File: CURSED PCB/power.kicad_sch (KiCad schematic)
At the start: 21 parts, among them J3 2 Wire Block for laser, J5 G125-MH104M4-04AD000P, U2 INA180, U4 SPX3819M5-L-3-3, U5 MCP1754S-3302xCB

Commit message: Small changes
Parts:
- F1: value 2A -> 1A
- J5: footprint canhw_footprints:HARWIN_G125-MH104M4-04AD000P -> canhw_footprints:connector_Harwin_G125-MH104M4-04AD000P
- gave numbers to parts that had none: 1
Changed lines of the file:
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@@
 			)
 		)
-		(property "Value" "2A"
+		(property "Value" "1A"
 			(at 53.34 53.34 90)
 			(effects
@@
 		(dnp no)
 		(fields_autoplaced yes)
-		(property "Reference" "U?"
+		(property "Reference" "U1"
 			(at 46.99 99.06 0)
 			(effects
@@
 			(project ""
 				(path "/9fb1a86f-679c-4b88-9ed1-932f4f414580/78e664bb-f661-4ad0-951c-8ffe0c2483d0"
-					(reference "U?")
+					(reference "U1")
 					(unit 1)
 				)
@@
 			)
 		)
-		(property "Footprint" "canhw_footprints:HARWIN_G125-MH104M4-04AD000P"
+		(property "Footprint" "canhw_footprints:connector_Harwin_G125-MH104M4-04AD000P"
 			(at 26.67 48.26 0)
 			(effects

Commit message: file
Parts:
- C10, C11, C12, C13, C8, C9: footprint Capacitor_SMD:C_0201_0603Metric_Pad0.64x0.40mm_HandSolder -> Capacitor_SMD:C_0603_1608Metric_Pad1.08x0.95mm_HandSolder
- R6: footprint Resistor_SMD:R_0201_0603Metric -> Resistor_SMD:R_0603_1608Metric_Pad0.98x0.95mm_HandSolder
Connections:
- net +3.3V is gone; now on net +3.3VD: U2.5 (V+)
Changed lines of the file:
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@@
 	)
 	(junction
-		(at 118.11 57.15)
-		(diameter 0)
-		(color 0 0 0 0)
-	)
-	(junction
 		(at 205.74 88.9)
 		(diameter 0)
@@
 	(wire
 		(pts
-			(xy 118.11 46.99) (xy 118.11 57.15)
+			(xy 90.17 45.72) (xy 90.17 57.15)
 		)
 		(stroke
@@
 	(wire
 		(pts
-			(xy 90.17 57.15) (xy 118.11 57.15)
+			(xy 203.2 54.61) (xy 214.63 54.61)
 		)
 		(stroke
@@
 	(wire
 		(pts
-			(xy 203.2 54.61) (xy 214.63 54.61)
+			(xy 205.74 88.9) (xy 219.71 88.9)
 		)
 		(stroke
@@
 	(wire
 		(pts
-			(xy 205.74 88.9) (xy 219.71 88.9)
+			(xy 90.17 57.15) (xy 153.67 57.15)
 		)
 		(stroke
@@
 	(wire
 		(pts
-			(xy 118.11 57.15) (xy 153.67 57.15)
-		)
-		(stroke
-			(width 0)
-			(type default)
-		)
-	)
-	(wire
-		(pts
 			(xy 198.12 96.52) (xy 198.12 99.06)
 		)
@@
 			)
 		)
-		(property "Value" "+3.3V"
+		(property "Value" "+3.3VD"
 			(at 95.25 44.45 0)
 			(effects
@@
 	(symbol
 		(lib_id "power:+3.3VA")
-		(at 118.11 46.99 0)
+		(at 90.17 45.72 0)
 		(unit 1)
 		(exclude_from_sim no)
@@
 		(fields_autoplaced yes)
 		(property "Reference" "#PWR022"
-			(at 118.11 50.8 0)
+			(at 90.17 49.53 0)
 			(effects
 				(font
@@
 		)
 		(property "Value" "+5V"
-			(at 118.11 41.91 0)
+			(at 90.17 40.64 0)
 			(effects
 				(font
@@
 		)
 		(property "Footprint" ""
-			(at 118.11 46.99 0)
+			(at 90.17 45.72 0)
 			(effects
 				(font
@@
 		)
 		(property "Datasheet" ""
-			(at 118.11 46.99 0)
+			(at 90.17 45.72 0)
 			(effects
 				(font
@@
 		)
 		(property "Description" "Power symbol creates a global label with name \"+3.3VA\""
-			(at 118.11 46.99 0)
+			(at 90.17 45.72 0)
 			(effects
 				(font
@@
 			)
 		)
-		(property "Footprint" "Capacitor_SMD:C_0201_0603Metric_Pad0.64x0.40mm_HandSolder"
+		(property "Footprint" "Capacitor_SMD:C_0603_1608Metric_Pad1.08x0.95mm_HandSolder"
 			(at 201.6252 68.58 0)
 			(effects
@@
 			)
 		)
-		(property "Footprint" "Capacitor_SMD:C_0201_0603Metric_Pad0.64x0.40mm_HandSolder"
+		(property "Footprint" "Capacitor_SMD:C_0603_1608Metric_Pad1.08x0.95mm_HandSolder"
 			(at 166.0652 96.52 0)
 			(effects
@@
 			)
 		)
-		(property "Footprint" "Capacitor_SMD:C_0201_0603Metric_Pad0.64x0.40mm_HandSolder"
+		(property "Footprint" "Capacitor_SMD:C_0603_1608Metric_Pad1.08x0.95mm_HandSolder"
 			(at 166.0652 62.23 0)
 			(effects
@@
 			)
 		)
-		(property "Footprint" "Capacitor_SMD:C_0201_0603Metric_Pad0.64x0.40mm_HandSolder"
+		(property "Footprint" "Capacitor_SMD:C_0603_1608Metric_Pad1.08x0.95mm_HandSolder"
 			(at 215.5952 66.04 0)
 			(effects
@@
 			)
 		)
-		(property "Footprint" "Resistor_SMD:R_0201_0603Metric"
+		(property "Footprint" "Resistor_SMD:R_0603_1608Metric_Pad0.98x0.95mm_HandSolder"
 			(at 84.074 56.134 90)
 			(effects
@@
 			)
 		)
-		(property "Footprint" "Capacitor_SMD:C_0201_0603Metric_Pad0.64x0.40mm_HandSolder"
+		(property "Footprint" "Capacitor_SMD:C_0603_1608Metric_Pad1.08x0.95mm_HandSolder"
 			(at 220.6752 96.52 0)
 			(effects
@@
 			)
 		)
-		(property "Footprint" "Capacitor_SMD:C_0201_0603Metric_Pad0.64x0.40mm_HandSolder"
+		(property "Footprint" "Capacitor_SMD:C_0603_1608Metric_Pad1.08x0.95mm_HandSolder"
 			(at 199.0852 96.52 0)
 			(effects

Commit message: connected stuff for pcb
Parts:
- added TP6: 5V, TestPoint:TestPoint_Loop_D2.50mm_Drill1.0mm, symbol Connector:TestPoint
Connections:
- net +5V: now also U2.4 (-), TP6.1; no longer U2.3 (+)
- net at F1.2, R6.1: now also U2.3 (+); no longer U2.4 (-)
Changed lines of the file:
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@@
-	)
-	(junction
-		(at 77.47 57.15)
-		(diameter 0)
-		(color 0 0 0 0)
 	)
 	(junction
@@
 	)
 	(junction
+		(at 78.74 57.15)
+		(diameter 0)
+		(color 0 0 0 0)
+	)
+	(junction
+		(at 99.06 57.15)
+		(diameter 0)
+		(color 0 0 0 0)
+	)
+	(junction
 		(at 205.74 88.9)
 		(diameter 0)
@@
 	(wire
 		(pts
-			(xy 90.17 77.47) (xy 77.47 77.47)
-		)
-		(stroke
-			(width 0)
-			(type default)
-		)
-	)
-	(wire
-		(pts
 			(xy 95.25 49.53) (xy 95.25 67.31)
 		)
@@
 	(wire
 		(pts
-			(xy 90.17 57.15) (xy 90.17 72.39)
-		)
-		(stroke
-			(width 0)
-			(type default)
-		)
-	)
-	(wire
-		(pts
 			(xy 54.61 106.68) (xy 54.61 86.36)
 		)
@@
 	(wire
 		(pts
+			(xy 88.9 77.47) (xy 90.17 77.47)
+		)
+		(stroke
+			(width 0)
+			(type default)
+		)
+	)
+	(wire
+		(pts
 			(xy 203.2 54.61) (xy 214.63 54.61)
 		)
@@
 	(wire
 		(pts
-			(xy 90.17 57.15) (xy 153.67 57.15)
+			(xy 90.17 57.15) (xy 99.06 57.15)
 		)
 		(stroke
@@
 	(wire
 		(pts
-			(xy 57.15 57.15) (xy 77.47 57.15)
+			(xy 57.15 57.15) (xy 78.74 57.15)
 		)
 		(stroke
@@
 	(wire
 		(pts
+			(xy 91.44 59.69) (xy 90.17 59.69)
+		)
+		(stroke
+			(width 0)
+			(type default)
+		)
+	)
+	(wire
+		(pts
 			(xy 95.25 82.55) (xy 95.25 87.63)
 		)
@@
 	(wire
 		(pts
+			(xy 78.74 72.39) (xy 78.74 57.15)
+		)
+		(stroke
+			(width 0)
+			(type default)
+		)
+	)
+	(wire
+		(pts
 			(xy 198.12 96.52) (xy 198.12 99.06)
 		)
@@
 	(wire
 		(pts
+			(xy 88.9 74.93) (xy 91.44 74.93)
+		)
+		(stroke
+			(width 0)
+			(type default)
+		)
+	)
+	(wire
+		(pts
 			(xy 29.21 109.22) (xy 39.37 109.22)
 		)
@@
 	(wire
 		(pts
+			(xy 78.74 57.15) (xy 80.01 57.15)
+		)
+		(stroke
+			(width 0)
+			(type default)
+		)
+	)
+	(wire
+		(pts
 			(xy 200.66 57.15) (xy 200.66 60.96)
 		)
@@
 	(wire
 		(pts
-			(xy 77.47 57.15) (xy 80.01 57.15)
-		)
-		(stroke
-			(width 0)
-			(type default)
-		)
-	)
-	(wire
-		(pts
 			(xy 46.99 116.84) (xy 46.99 120.65)
 		)
@@
 	(wire
 		(pts
+			(xy 91.44 74.93) (xy 91.44 59.69)
+		)
+		(stroke
+			(width 0)
+			(type default)
+		)
+	)
+	(wire
+		(pts
 			(xy 45.72 86.36) (xy 54.61 86.36)
 		)
@@
 	(wire
 		(pts
-			(xy 77.47 77.47) (xy 77.47 57.15)
-		)
-		(stroke
-			(width 0)
-			(type default)
-		)
-	)
-	(wire
-		(pts
 			(xy 153.67 88.9) (xy 165.1 88.9)
 		)
@@
 	(wire
 		(pts
+			(xy 78.74 72.39) (xy 90.17 72.39)
+		)
+		(stroke
+			(width 0)
+			(type default)
+		)
+	)
+	(wire
+		(pts
 			(xy 29.21 57.15) (xy 49.53 57.15)
 		)
@@
 		(pts
 			(xy 214.63 54.61) (xy 214.63 58.42)
+		)
+		(stroke
+			(width 0)
+			(type default)
+		)
+	)
+	(wire
+		(pts
+			(xy 90.17 59.69) (xy 90.17 57.15)
+		)
+		(stroke
+			(width 0)
+			(type default)
+		)
+	)
+	(wire
+		(pts
+			(xy 99.06 57.15) (xy 153.67 57.15)
+		)
+		(stroke
+			(width 0)
+			(type default)
+		)
+	)
+	(wire
+		(pts
+			(xy 88.9 77.47) (xy 88.9 74.93)
 		)
 		(stroke
@@
 					(unit 1)
 				)
+			)
+		)
+	)
+	(symbol
+		(lib_id "Connector:TestPoint")
+		(at 99.06 57.15 0)
+		(unit 1)
+		(exclude_from_sim no)
+		(in_bom yes)
+		(on_board yes)
+		(dnp no)
+		(property "Reference" "TP6"
+			(at 101.6 52.832 0)
+			(effects
+				(font
+					(size 1.27 1.27)
+				)
+				(justify left)
+			)
+		)
+		(property "Value" "5V"
+			(at 101.6 55.1179 0)
+			(effects
+				(font
+					(size 1.27 1.27)
+				)
+				(justify left)
+			)
+		)
+		(property "Footprint" "TestPoint:TestPoint_Loop_D2.50mm_Drill1.0mm"
+			(at 104.14 57.15 0)
+			(effects
+				(font
+					(size 1.27 1.27)
+				)
+				(hide yes)
+			)
+		)
+		(property "Datasheet" "~"
+			(at 104.14 57.15 0)
+			(effects
+				(font
+					(size 1.27 1.27)
+				)
+				(hide yes)
+			)
+		)
+		(property "Description" "test point"
+			(at 99.06 57.15 0)
+			(effects
+				(font
+					(size 1.27 1.27)
+				)
+				(hide yes)
+			)
+		)
+		(pin "1"
+		)
+		(instances
+			(project "sensor_1"
+				(path "/9fb1a86f-679c-4b88-9ed1-932f4f414580/78e664bb-f661-4ad0-951c-8ffe0c2483d0"
+					(reference "TP6")
+					(unit 1)
+				)

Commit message: wire
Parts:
- F1: value 1A -> 1.5A
- R6: value 165m -> 198m
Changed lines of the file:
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@@
 			)
 		)
-		(property "Value" "1A"
+		(property "Value" "1.5A"
 			(at 53.34 53.34 90)
 			(effects
@@
 			)
 		)
-		(property "Value" "165m"
+		(property "Value" "198m"
 			(at 83.82 53.34 90)
 			(effects

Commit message: redone pcb
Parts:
- C10, C11, C12, C13, C8, C9: footprint Capacitor_SMD:C_0603_1608Metric_Pad1.08x0.95mm_HandSolder -> Capacitor_SMD:C_0805_2012Metric_Pad1.18x1.45mm_HandSolder
- H1, H2, H3, H4: footprint MountingHole:MountingHole_2.2mm_M2_DIN965_Pad -> MountingHole:MountingHole_3.2mm_M3_DIN965_Pad
- R6: footprint Resistor_SMD:R_0603_1608Metric_Pad0.98x0.95mm_HandSolder -> Resistor_SMD:R_0805_2012Metric_Pad1.20x1.40mm_HandSolder
- TP2, TP3, TP6: footprint TestPoint:TestPoint_Loop_D2.50mm_Drill1.0mm -> TestPoint:TestPoint_Pad_1.5x1.5mm
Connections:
- net GND: no longer C10.2, C13.2, C9.2, H2.1, U5.1 (GND)
- new net AGND: C10.2, C13.2, C9.2, H2.1, U5.1 (GND)
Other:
- moved on the sheet: H2
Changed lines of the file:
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@@
 	)
 	(junction
-		(at 80.01 116.84)
-		(diameter 0)
-		(color 0 0 0 0)
-	)
-	(junction
 		(at 153.67 57.15)
 		(diameter 0)
@@
 	(wire
 		(pts
-			(xy 68.58 116.84) (xy 80.01 116.84)
-		)
-		(stroke
-			(width 0)
-			(type default)
-		)
-	)
-	(wire
-		(pts
 			(xy 153.67 88.9) (xy 165.1 88.9)
 		)
@@
 	(wire
 		(pts
-			(xy 80.01 116.84) (xy 90.17 116.84)
+			(xy 68.58 116.84) (xy 90.17 116.84)
 		)
 		(stroke
@@
 	(wire
 		(pts
+			(xy 80.01 114.3) (xy 80.01 121.92)
+		)
+		(stroke
+			(width 0)
+			(type default)
+		)
+	)
+	(wire
+		(pts
 			(xy 99.06 57.15) (xy 153.67 57.15)
 		)
@@
 			)
 		)
-		(property "Value" "GND"
-			(at 185.42 104.14 0)
+		(property "Value" "AGND"
+			(at 187.96 100.3299 0)
 			(effects
 				(font
 					(size 1.27 1.27)
 				)
+				(justify left)
 			)
 		)
@@
 	(symbol
 		(lib_id "Mechanical:MountingHole_Pad")
-		(at 80.01 114.3 0)
+		(at 80.01 111.76 0)
 		(unit 1)
 		(exclude_from_sim no)
@@
 		(fields_autoplaced yes)
 		(property "Reference" "H2"
-			(at 82.55 111.7599 0)
+			(at 82.55 109.2199 0)
 			(effects
 				(font
@@
 		)
 		(property "Value" "MH2"
-			(at 82.55 114.2999 0)
+			(at 82.55 111.7599 0)
 			(effects
 				(font
@@
 			)
 		)
-		(property "Footprint" "MountingHole:MountingHole_2.2mm_M2_DIN965_Pad"
-			(at 80.01 114.3 0)
+		(property "Footprint" "MountingHole:MountingHole_3.2mm_M3_DIN965_Pad"
+			(at 80.01 111.76 0)
 			(effects
 				(font
@@
 		)
 		(property "Datasheet" "~"
-			(at 80.01 114.3 0)
+			(at 80.01 111.76 0)
 			(effects
 				(font
@@
 		)
 		(property "Description" "Mounting Hole with connection"
-			(at 80.01 114.3 0)
+			(at 80.01 111.76 0)
 			(effects
 				(font
@@
 			)
 		)
-		(property "Value" "GND"
-			(at 198.12 104.14 0)
+		(property "Value" "AGND"
+			(at 200.66 100.3299 0)
 			(effects
 				(font
 					(size 1.27 1.27)
 				)
+				(justify left)
 			)
 		)
@@
 	(symbol
 		(lib_id "power:GND")
+		(at 80.01 121.92 0)
+		(unit 1)
+		(exclude_from_sim no)
+		(in_bom yes)
+		(on_board yes)
+		(dnp no)
+		(fields_autoplaced yes)
+		(property "Reference" "#PWR01"
+			(at 80.01 128.27 0)
+			(effects
+				(font
+					(size 1.27 1.27)
+				)
+				(hide yes)
+			)
+		)
+		(property "Value" "AGND"
+			(at 80.01 127 0)
+			(effects
+				(font
+					(size 1.27 1.27)
+				)
+			)
+		)
+		(property "Footprint" ""
+			(at 80.01 121.92 0)
+			(effects
+				(font
+					(size 1.27 1.27)
+				)
+				(hide yes)
+			)
+		)
+		(property "Datasheet" ""
+			(at 80.01 121.92 0)
+			(effects
+				(font
+					(size 1.27 1.27)
+				)
+				(hide yes)
+			)
+		)
+		(property "Description" "Power symbol creates a global label with name \"GND\" , ground"
+			(at 80.01 121.92 0)
+			(effects
+				(font
+					(size 1.27 1.27)
+				)
+				(hide yes)
+			)
+		)
+		(pin "1"
+		)
+		(instances
+			(project "sensor_1"
+				(path "/9fb1a86f-679c-4b88-9ed1-932f4f414580/78e664bb-f661-4ad0-951c-8ffe0c2483d0"
+					(reference "#PWR01")
+					(unit 1)
+				)
+			)
+		)
+	)
+	(symbol
+		(lib_id "power:GND")
 		(at 46.99 67.31 0)
 		(unit 1)
@@
 			)
 		)
-		(property "Footprint" "TestPoint:TestPoint_Loop_D2.50mm_Drill1.0mm"
+		(property "Footprint" "TestPoint:TestPoint_Pad_1.5x1.5mm"
 			(at 208.28 54.61 0)
 			(effects
@@
 			)
 		)
-		(property "Footprint" "MountingHole:MountingHole_2.2mm_M2_DIN965_Pad"
+		(property "Footprint" "MountingHole:MountingHole_3.2mm_M3_DIN965_Pad"
 			(at 90.17 114.3 0)
 			(effects
@@
 			)
 		)
-		(property "Footprint" "Capacitor_SMD:C_0603_1608Metric_Pad1.08x0.95mm_HandSolder"
+		(property "Footprint" "Capacitor_SMD:C_0805_2012Metric_Pad1.18x1.45mm_HandSolder"
 			(at 201.6252 68.58 0)
 			(effects
@@
 			)
 		)
-		(property "Footprint" "Capacitor_SMD:C_0603_1608Metric_Pad1.08x0.95mm_HandSolder"
+		(property "Footprint" "Capacitor_SMD:C_0805_2012Metric_Pad1.18x1.45mm_HandSolder"
 			(at 166.0652 96.52 0)
 			(effects
@@
 			)
 		)
-		(property "Footprint" "MountingHole:MountingHole_2.2mm_M2_DIN965_Pad"
+		(property "Footprint" "MountingHole:MountingHole_3.2mm_M3_DIN965_Pad"
 			(at 101.6 114.3 0)
 			(effects
@@
 			)
 		)
-		(property "Footprint" "TestPoint:TestPoint_Loop_D2.50mm_Drill1.0mm"
+		(property "Footprint" "TestPoint:TestPoint_Pad_1.5x1.5mm"
 			(at 210.82 88.9 0)
 			(effects
@@
 			)
 		)
-		(property "Footprint" "TestPoint:TestPoint_Loop_D2.50mm_Drill1.0mm"
+		(property "Footprint" "TestPoint:TestPoint_Pad_1.5x1.5mm"
 			(at 104.14 57.15 0)
 			(effects
@@
 			)
 		)
-		(property "Footprint" "Capacitor_SMD:C_0603_1608Metric_Pad1.08x0.95mm_HandSolder"
+		(property "Footprint" "Capacitor_SMD:C_0805_2012Metric_Pad1.18x1.45mm_HandSolder"
 			(at 166.0652 62.23 0)
 			(effects
@@
 			)
 		)
-		(property "Value" "GND"
-			(at 219.71 104.14 0)
+		(property "Value" "AGND"
+			(at 222.25 100.3299 0)
 			(effects
 				(font
 					(size 1.27 1.27)
 				)
+				(justify left)
 			)
 		)
@@
 			)
 		)
-		(property "Footprint" "Capacitor_SMD:C_0603_1608Metric_Pad1.08x0.95mm_HandSolder"
+		(property "Footprint" "Capacitor_SMD:C_0805_2012Metric_Pad1.18x1.45mm_HandSolder"
 			(at 215.5952 66.04 0)
 			(effects
@@
 			)
 		)
-		(property "Footprint" "Resistor_SMD:R_0603_1608Metric_Pad0.98x0.95mm_HandSolder"
+		(property "Footprint" "Resistor_SMD:R_0805_2012Metric_Pad1.20x1.40mm_HandSolder"
 			(at 84.074 56.134 90)
 			(effects
@@
 			)
 		)
-		(property "Footprint" "Capacitor_SMD:C_0603_1608Metric_Pad1.08x0.95mm_HandSolder"
+		(property "Footprint" "Capacitor_SMD:C_0805_2012Metric_Pad1.18x1.45mm_HandSolder"
 			(at 220.6752 96.52 0)
 			(effects
@@
 			)
 		)
-		(property "Footprint" "MountingHole:MountingHole_2.2mm_M2_DIN965_Pad"
+		(property "Footprint" "MountingHole:MountingHole_3.2mm_M3_DIN965_Pad"
 			(at 68.58 114.3 0)
 			(effects
@@
 			)
 		)
-		(property "Footprint" "Capacitor_SMD:C_0603_1608Metric_Pad1.08x0.95mm_HandSolder"
+		(property "Footprint" "Capacitor_SMD:C_0805_2012Metric_Pad1.18x1.45mm_HandSolder"
 			(at 199.0852 96.52 0)
 			(effects
@@
 			)
 		)
-		(property "Value" "GND"
-			(at 165.1 104.14 0)
+		(property "Value" "AGND"
+			(at 167.64 100.3299 0)
 			(effects
 				(font
 					(size 1.27 1.27)
 				)
+				(justify left)
 			)
 		)

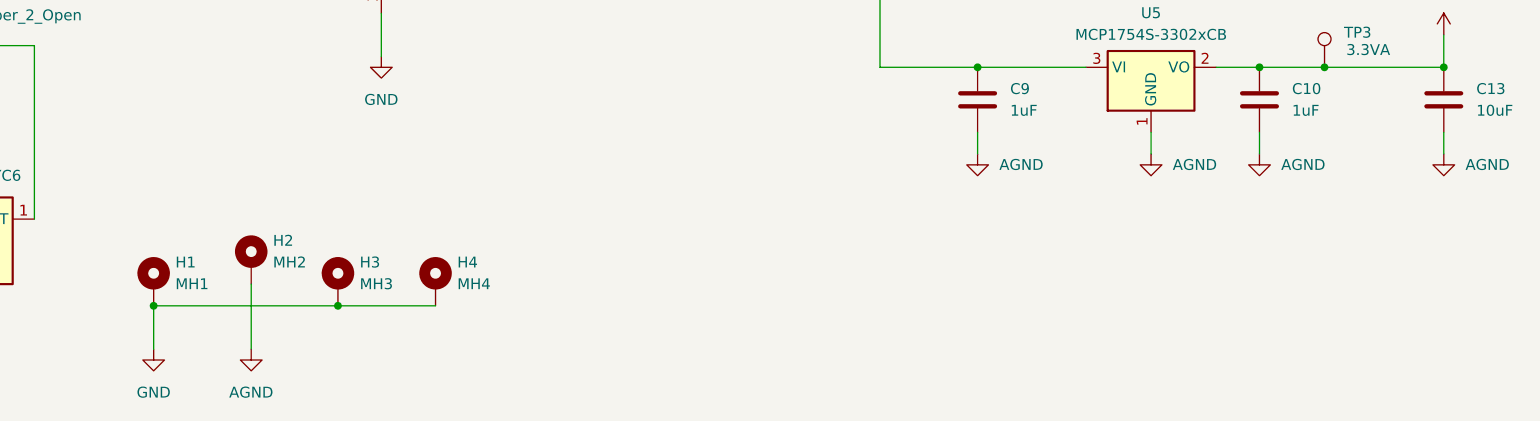
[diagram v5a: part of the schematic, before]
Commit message: no spilt-ground plane (bad idea)
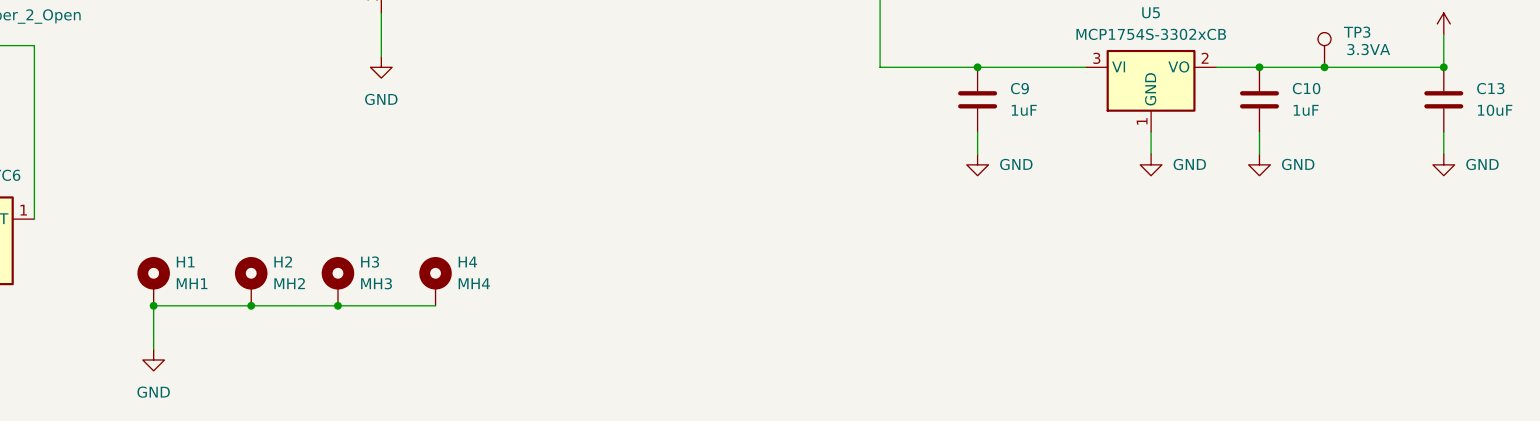
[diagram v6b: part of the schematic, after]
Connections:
- net AGND is gone; now on net GND: C10.2, C13.2, C9.2, H2.1, U5.1 (GND)
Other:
- moved on the sheet: H2
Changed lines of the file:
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@@
 	)
 	(junction
+		(at 80.01 116.84)
+		(diameter 0)
+		(color 0 0 0 0)
+	)
+	(junction
 		(at 198.12 88.9)
 		(diameter 0)
@@
 	(wire
 		(pts
-			(xy 105.41 74.93) (xy 114.3 74.93)
+			(xy 80.01 116.84) (xy 90.17 116.84)
 		)
 		(stroke
@@
 	(wire
 		(pts
-			(xy 68.58 116.84) (xy 90.17 116.84)
+			(xy 105.41 74.93) (xy 114.3 74.93)
 		)
 		(stroke
@@
 	(wire
 		(pts
-			(xy 214.63 66.04) (xy 214.63 68.58)
+			(xy 68.58 116.84) (xy 80.01 116.84)
 		)
 		(stroke
@@
 	(wire
 		(pts
-			(xy 29.21 59.69) (xy 46.99 59.69)
+			(xy 214.63 66.04) (xy 214.63 68.58)
 		)
 		(stroke
@@
 	(wire
 		(pts
-			(xy 173.99 54.61) (xy 177.8 54.61)
+			(xy 29.21 59.69) (xy 46.99 59.69)
 		)
 		(stroke
@@
 	(wire
 		(pts
-			(xy 153.67 57.15) (xy 153.67 54.61)
+			(xy 173.99 54.61) (xy 177.8 54.61)
 		)
 		(stroke
@@
 	(wire
 		(pts
-			(xy 214.63 54.61) (xy 214.63 58.42)
+			(xy 153.67 57.15) (xy 153.67 54.61)
 		)
 		(stroke
@@
 	(wire
 		(pts
-			(xy 90.17 59.69) (xy 90.17 57.15)
+			(xy 214.63 54.61) (xy 214.63 58.42)
 		)
 		(stroke
@@
 	(wire
 		(pts
-			(xy 80.01 114.3) (xy 80.01 121.92)
+			(xy 90.17 59.69) (xy 90.17 57.15)
 		)
 		(stroke
@@
 			)
 		)
-		(property "Value" "AGND"
+		(property "Value" "GND"
 			(at 187.96 100.3299 0)
 			(effects
@@
 	(symbol
 		(lib_id "Mechanical:MountingHole_Pad")
-		(at 80.01 111.76 0)
+		(at 80.01 114.3 0)
 		(unit 1)
 		(exclude_from_sim no)
@@
 		(fields_autoplaced yes)
 		(property "Reference" "H2"
-			(at 82.55 109.2199 0)
+			(at 82.55 111.7599 0)
 			(effects
 				(font
@@
 		)
 		(property "Value" "MH2"
-			(at 82.55 111.7599 0)
+			(at 82.55 114.2999 0)
 			(effects
 				(font
@@
 		)
 		(property "Footprint" "MountingHole:MountingHole_3.2mm_M3_DIN965_Pad"
-			(at 80.01 111.76 0)
+			(at 80.01 114.3 0)
 			(effects
 				(font
@@
 		)
 		(property "Datasheet" "~"
-			(at 80.01 111.76 0)
+			(at 80.01 114.3 0)
 			(effects
 				(font
@@
 		)
 		(property "Description" "Mounting Hole with connection"
-			(at 80.01 111.76 0)
+			(at 80.01 114.3 0)
 			(effects
 				(font
@@
 			)
 		)
-		(property "Value" "AGND"
+		(property "Value" "GND"
 			(at 200.66 100.3299 0)
 			(effects
@@
 	(symbol
 		(lib_id "power:GND")
-		(at 80.01 121.92 0)
-		(unit 1)
-		(exclude_from_sim no)
-		(in_bom yes)
-		(on_board yes)
-		(dnp no)
-		(fields_autoplaced yes)
-		(property "Reference" "#PWR01"
-			(at 80.01 128.27 0)
-			(effects
-				(font
-					(size 1.27 1.27)
-				)
-				(hide yes)
-			)
-		)
-		(property "Value" "AGND"
-			(at 80.01 127 0)
-			(effects
-				(font
-					(size 1.27 1.27)
-				)
-			)
-		)
-		(property "Footprint" ""
-			(at 80.01 121.92 0)
-			(effects
-				(font
-					(size 1.27 1.27)
-				)
-				(hide yes)
-			)
-		)
-		(property "Datasheet" ""
-			(at 80.01 121.92 0)
-			(effects
-				(font
-					(size 1.27 1.27)
-				)
-				(hide yes)
-			)
-		)
-		(property "Description" "Power symbol creates a global label with name \"GND\" , ground"
-			(at 80.01 121.92 0)
-			(effects
-				(font
-					(size 1.27 1.27)
-				)
-				(hide yes)
-			)
-		)
-		(pin "1"
-		)
-		(instances
-			(project "sensor_1"
-				(path "/9fb1a86f-679c-4b88-9ed1-932f4f414580/78e664bb-f661-4ad0-951c-8ffe0c2483d0"
-					(reference "#PWR01")
-					(unit 1)
-				)
-			)
-		)
-	)
-	(symbol
-		(lib_id "power:GND")
 		(at 46.99 67.31 0)
 		(unit 1)
@@
 			)
 		)
-		(property "Value" "AGND"
+		(property "Value" "GND"
 			(at 222.25 100.3299 0)
 			(effects
@@
 			)
 		)
-		(property "Value" "AGND"
+		(property "Value" "GND"
 			(at 167.64 100.3299 0)
 			(effects

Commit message: fixes from darian review
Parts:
- F1: value 1.5A -> 600mA
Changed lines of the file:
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@@
 			)
 		)
-		(property "Value" "1.5A"
+		(property "Value" "600mA"
 			(at 53.34 53.34 90)
 			(effects
